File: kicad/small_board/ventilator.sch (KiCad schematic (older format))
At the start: 53 parts, among them J1 PJ-202A, J2 Conn_01x02, J3 Conn_01x02, J4 Conn_01x02, J5 Conn_01x02, J6 Conn_01x02, J7 Conn_01x02, J8 Conn_01x02, J9 Conn_01x02, Q1 IRLIZ44NPBF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

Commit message: decent placement for kicad small board
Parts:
- added H1, H2, H3, H4: MountingHole_Pad, MountingHole:MountingHole_2.2mm_M2, symbol Mechanical:MountingHole_Pad
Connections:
- net GND: now also H1.1, H2.1, H3.1, H4.1
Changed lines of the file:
@@
 	4350 5150 4650 5150
 Wire Wire Line
+	4350 6550 4350 6800
+Wire Wire Line
 	4650 2000 4650 2100
 Wire Wire Line
@@
 	4750 4550 4650 4550
 Wire Wire Line
+	4750 6550 4750 6800
+Wire Wire Line
 	4900 1300 4900 1400
 Wire Wire Line
@@
 Wire Wire Line
 	5150 4100 5050 4100
+Wire Wire Line
+	5150 6550 5150 6800
+Wire Wire Line
+	5550 6550 5550 6800
 Wire Wire Line
 	6250 1950 5900 1950
@@
 $EndComp
 $Comp
+L power:GND #PWR0104
+U 1 1 5E8735F7
+P 4350 6800
+F 0 "#PWR0104" H 4350 6550 50  0001 C CNN
+F 1 "GND" H 4350 6646 50  0000 C CNN
+F 2 "" H 4350 6800 50  0001 C CNN
+F 3 "" H 4350 6800 50  0001 C CNN
+	1    4350 6800
+	1    0    0    -1
+$EndComp
+$Comp
+L power:GND #PWR0103
+U 1 1 5E874652
+P 4750 6800
+F 0 "#PWR0103" H 4750 6550 50  0001 C CNN
+F 1 "GND" H 4750 6646 50  0000 C CNN
+F 2 "" H 4750 6800 50  0001 C CNN
+F 3 "" H 4750 6800 50  0001 C CNN
+	1    4750 6800
+	1    0    0    -1
+$EndComp
+$Comp
 L power:GND #PWR016
 U 1 1 5E86C9CC
@@
 F 3 "" H 5050 5200 50  0001 C CNN
 	1    5050 5200
+	1    0    0    -1
+$EndComp
+$Comp
+L power:GND #PWR0102
+U 1 1 5E8751C6
+P 5150 6800
+F 0 "#PWR0102" H 5150 6550 50  0001 C CNN
+F 1 "GND" H 5150 6646 50  0000 C CNN
+F 2 "" H 5150 6800 50  0001 C CNN
+F 3 "" H 5150 6800 50  0001 C CNN
+	1    5150 6800
+	1    0    0    -1
+$EndComp
+$Comp
+L power:GND #PWR0101
+U 1 1 5E8756FC
+P 5550 6800
+F 0 "#PWR0101" H 5550 6550 50  0001 C CNN
+F 1 "GND" H 5550 6646 50  0000 C CNN
+F 2 "" H 5550 6800 50  0001 C CNN
+F 3 "" H 5550 6800 50  0001 C CNN
+	1    5550 6800
 	1    0    0    -1
 $EndComp
@@
 	1    0    0    -1
 $EndComp
+$Comp
+L Mechanical:MountingHole_Pad H1
+U 1 1 5E86D998
+P 4350 6450
+F 0 "H1" H 4450 6447 50  0000 L CNN
+F 1 "MountingHole_Pad" H 4450 6492 50  0001 L CNN
+F 2 "MountingHole:MountingHole_2.2mm_M2" H 4350 6450 50  0001 C CNN
+F 3 "~" H 4350 6450 50  0001 C CNN
+	1    4350 6450
+	1    0    0    -1
+$EndComp
+$Comp
+L Mechanical:MountingHole_Pad H2
+U 1 1 5E86E6A0
+P 4750 6450
+F 0 "H2" H 4850 6447 50  0000 L CNN
+F 1 "MountingHole_Pad" H 4850 6492 50  0001 L CNN
+F 2 "MountingHole:MountingHole_2.2mm_M2" H 4750 6450 50  0001 C CNN
+F 3 "~" H 4750 6450 50  0001 C CNN
+	1    4750 6450
+	1    0    0    -1
+$EndComp
+$Comp
+L Mechanical:MountingHole_Pad H3
+U 1 1 5E8700AE
+P 5150 6450
+F 0 "H3" H 5250 6447 50  0000 L CNN
+F 1 "MountingHole_Pad" H 5250 6492 50  0001 L CNN
+F 2 "MountingHole:MountingHole_2.2mm_M2" H 5150 6450 50  0001 C CNN
+F 3 "~" H 5150 6450 50  0001 C CNN
+	1    5150 6450
+	1    0    0    -1
+$EndComp
+$Comp
+L Mechanical:MountingHole_Pad H4
+U 1 1 5E870B72
+P 5550 6450
+F 0 "H4" H 5650 6447 50  0000 L CNN
+F 1 "MountingHole_Pad" H 5650 6492 50  0001 L CNN
+F 2 "MountingHole:MountingHole_2.2mm_M2" H 5550 6450 50  0001 C CNN
+F 3 "~" H 5550 6450 50  0001 C CNN
+	1    5550 6450
+	1    0    0    -1
+$EndComp

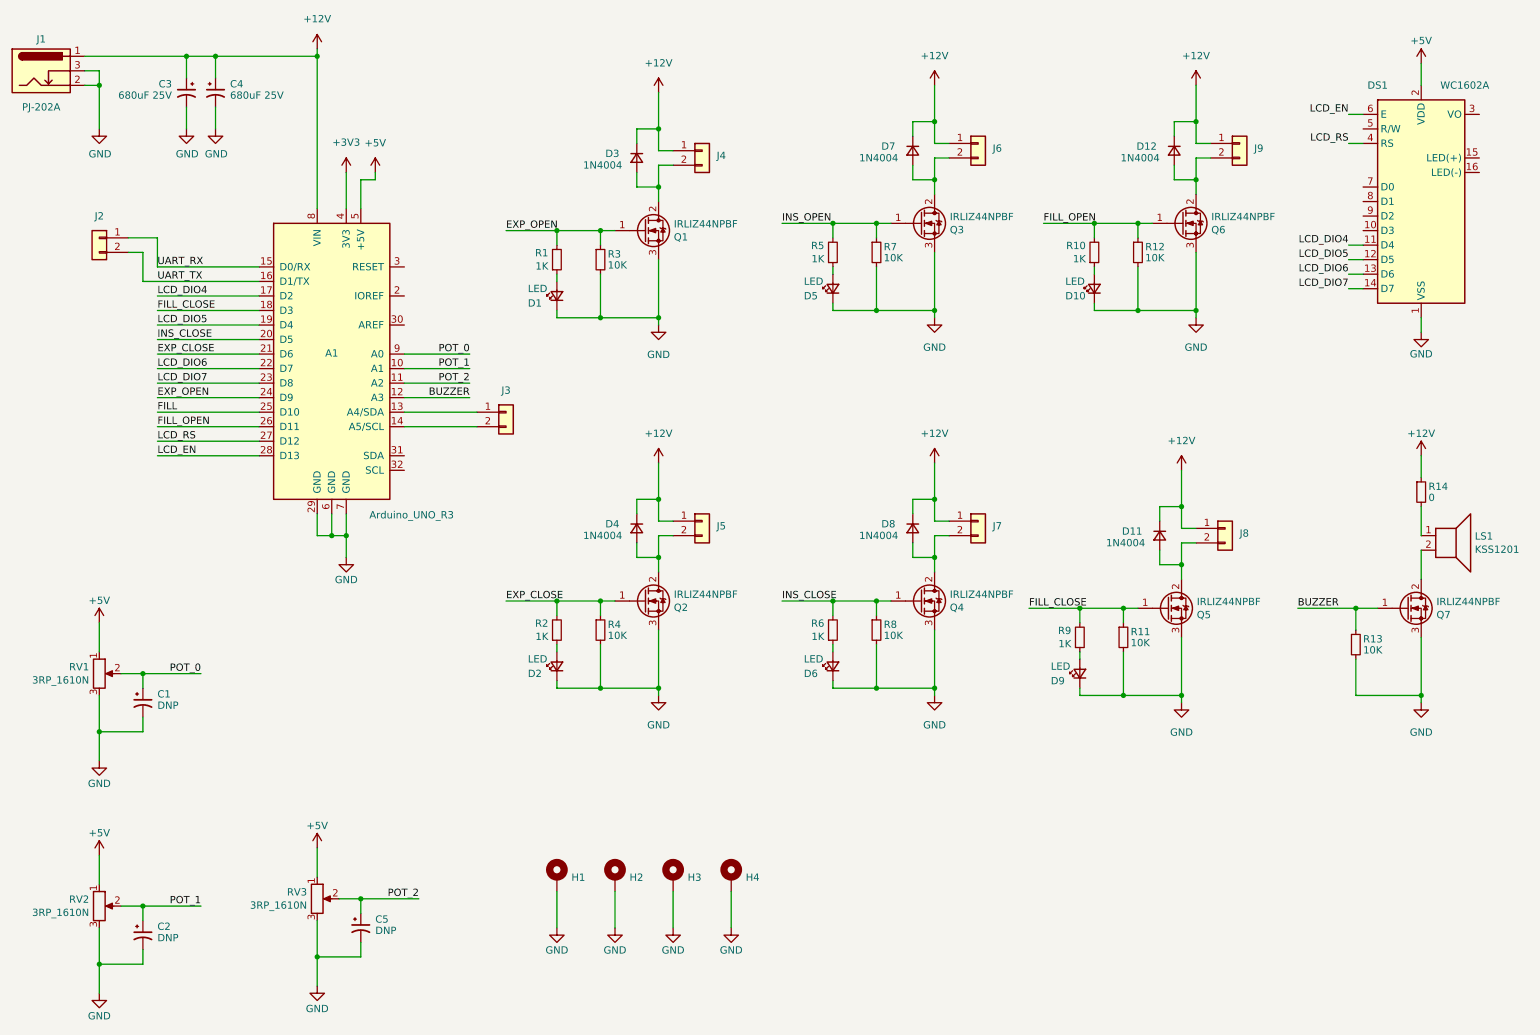
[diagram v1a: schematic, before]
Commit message: finishes layout of small kicad PCB
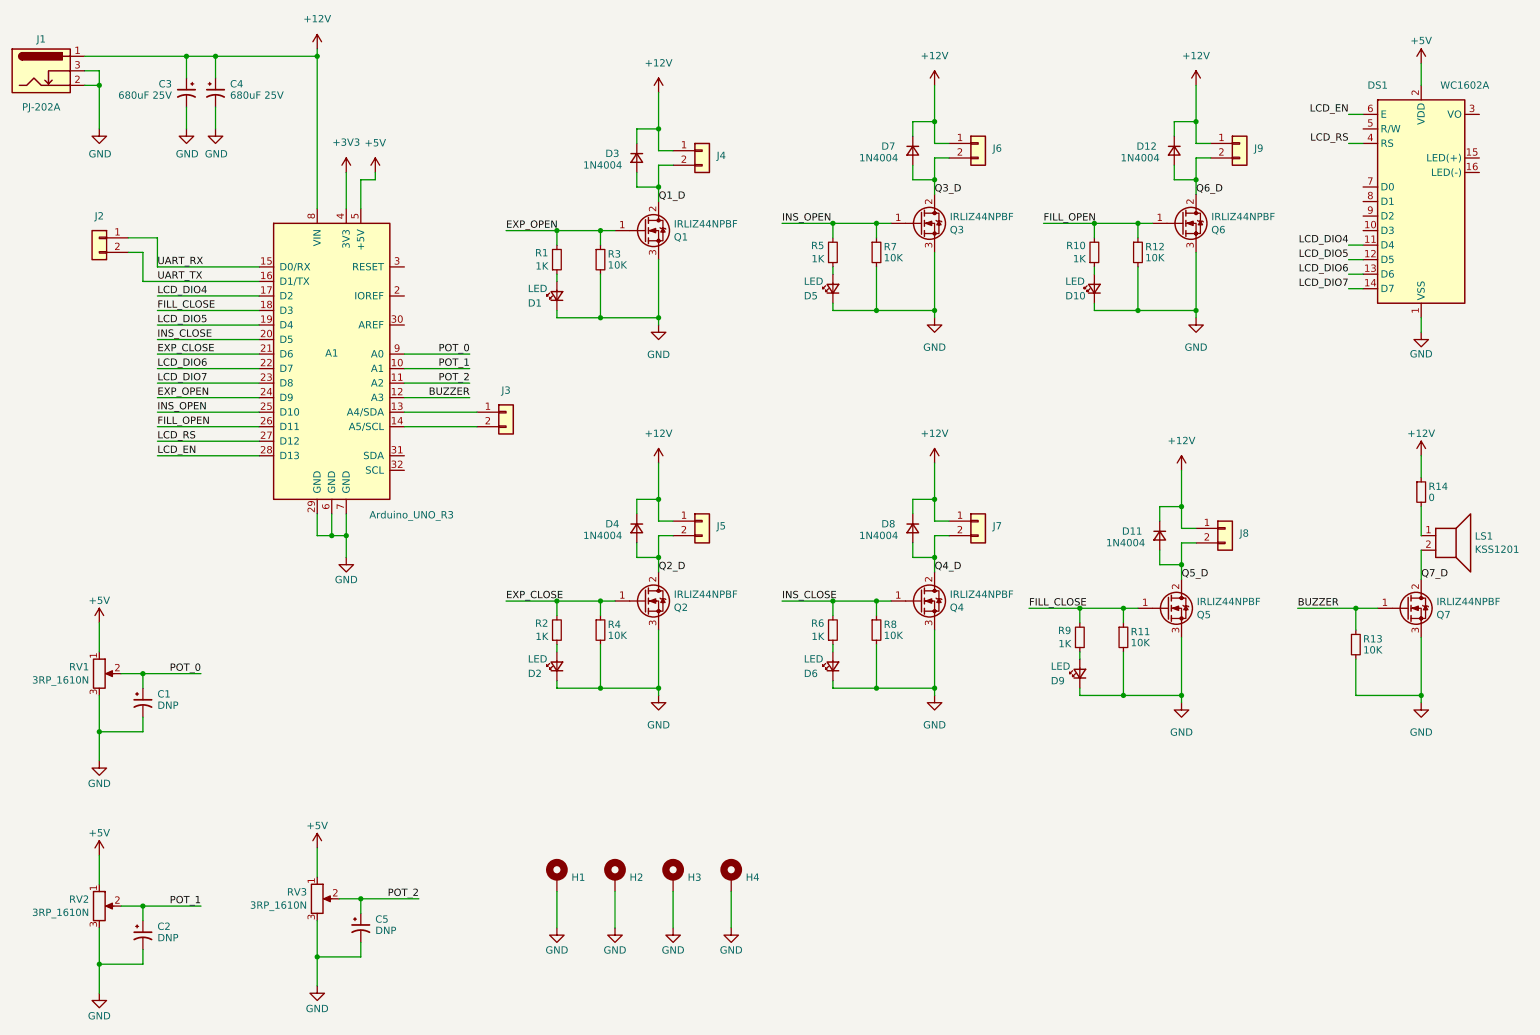
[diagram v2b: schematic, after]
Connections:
- net FILL is gone; now on net INS_OPEN: A1.25 (D10)
- net Q3_D: now reaches D7.2 (A), J6.2 (Pin_2), Q3.2 (D)
- net Q2_D: now reaches D4.2 (A), J5.2 (Pin_2), Q2.2 (D)
- net Q4_D: now reaches D8.2 (A), J7.2 (Pin_2), Q4.2 (D)
- net Q5_D: now reaches D11.2 (A), J8.2 (Pin_2), Q5.2 (D)
- net Q6_D: now reaches D12.2 (A), J9.2 (Pin_2), Q6.2 (D)
- net Q1_D: now reaches D3.2 (A), J4.2 (Pin_2), Q1.2 (D)
- net Q7_D: now reaches LS1.2, Q7.2 (D)
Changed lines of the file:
@@
 EXP_OPEN
 Text Label 1600 3250 0    50   ~ 0
-FILL
+INS_OPEN
 Text Label 1600 3350 0    50   ~ 0
 FILL_OPEN
@@
 Text Label 4000 4550 0    50   ~ 0
 EXP_CLOSE
+Text Label 5050 1800 0    50   ~ 0
+Q1_D
+Text Label 5050 4350 0    50   ~ 0
+Q2_D
 Text Label 5900 1950 0    50   ~ 0
 INS_OPEN
 Text Label 5900 4550 0    50   ~ 0
 INS_CLOSE
+Text Label 6950 1750 0    50   ~ 0
+Q3_D
+Text Label 6950 4350 0    50   ~ 0
+Q4_D
 Text Label 7600 4600 0    50   ~ 0
 FILL_CLOSE
 Text Label 7700 1950 0    50   ~ 0
 FILL_OPEN
+Text Label 8650 4400 0    50   ~ 0
+Q5_D
+Text Label 8750 1750 0    50   ~ 0
+Q6_D
 Text Label 9450 4600 0    50   ~ 0
 BUZZER
@@
 Text Label 9800 2400 2    50   ~ 0
 LCD_DIO7
+Text Label 10300 4400 0    50   ~ 0
+Q7_D
 $Comp
 L power:+5V #PWR03

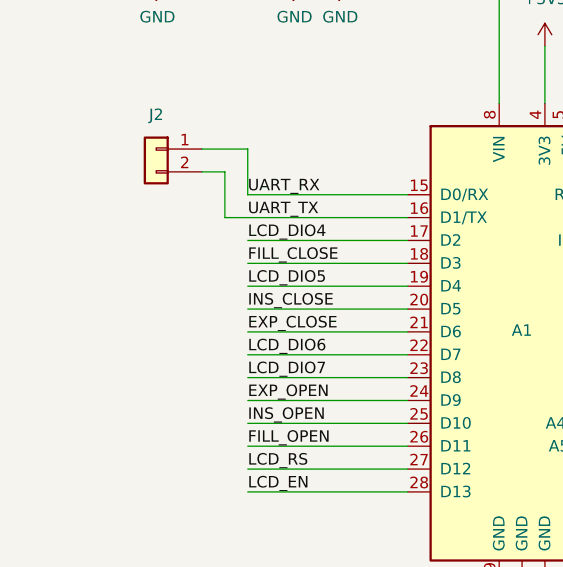
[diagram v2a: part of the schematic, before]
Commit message: fixes transistor order, adds ground test point
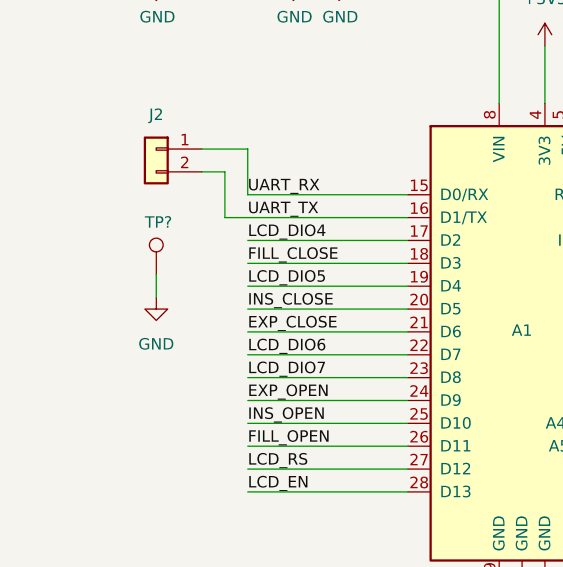
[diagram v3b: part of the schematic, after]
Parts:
- added TP?: TestPoint, Connector_PinHeader_2.54mm:PinHeader_1x01_P2.54mm_Horizontal, symbol Connector:TestPoint
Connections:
- net GND: now also TP?.1
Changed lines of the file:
@@
 	1200 1000 1200 1300
+Wire Wire Line
+	1200 2600 1200 2700
 Wire Wire Line
 	1200 4700 1200 4900
@@
 Q7_D
 $Comp
+L Connector:TestPoint TP?
+U 1 1 5E86FE32
+P 1200 2600
+F 0 "TP?" H 1150 2829 50  0000 L CNN
+F 1 "TestPoint" H 1258 2573 50  0001 L CNN
+F 2 "Connector_PinHeader_2.54mm:PinHeader_1x01_P2.54mm_Horizontal" H 1400 2600 50  0001 C CNN
+F 3 "~" H 1400 2600 50  0001 C CNN
+	1    1200 2600
+	1    0    0    -1
+$EndComp
+$Comp
 L power:+5V #PWR03
 U 1 1 5E84D8ED
@@
 	1    0    0    -1
 $EndComp
+$Comp
+L power:GND #PWR?
+U 1 1 5E871D76
+P 1200 2700
+F 0 "#PWR?" H 1200 2450 50  0001 C CNN
+F 1 "GND" H 1200 2496 50  0000 C CNN
+F 2 "" H 1200 2700 50  0001 C CNN
+F 3 "" H 1200 2700 50  0001 C CNN
+	1    1200 2700
+	1    0    0    -1
+$EndComp
